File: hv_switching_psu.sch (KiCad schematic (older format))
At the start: 19 parts, among them P1 CONN_2, P2 CONN_2, P3 CONN_2, P4 CONN_1, SW1 SWITCH_INV, T1 IRF644PBF, U1 MAX1771

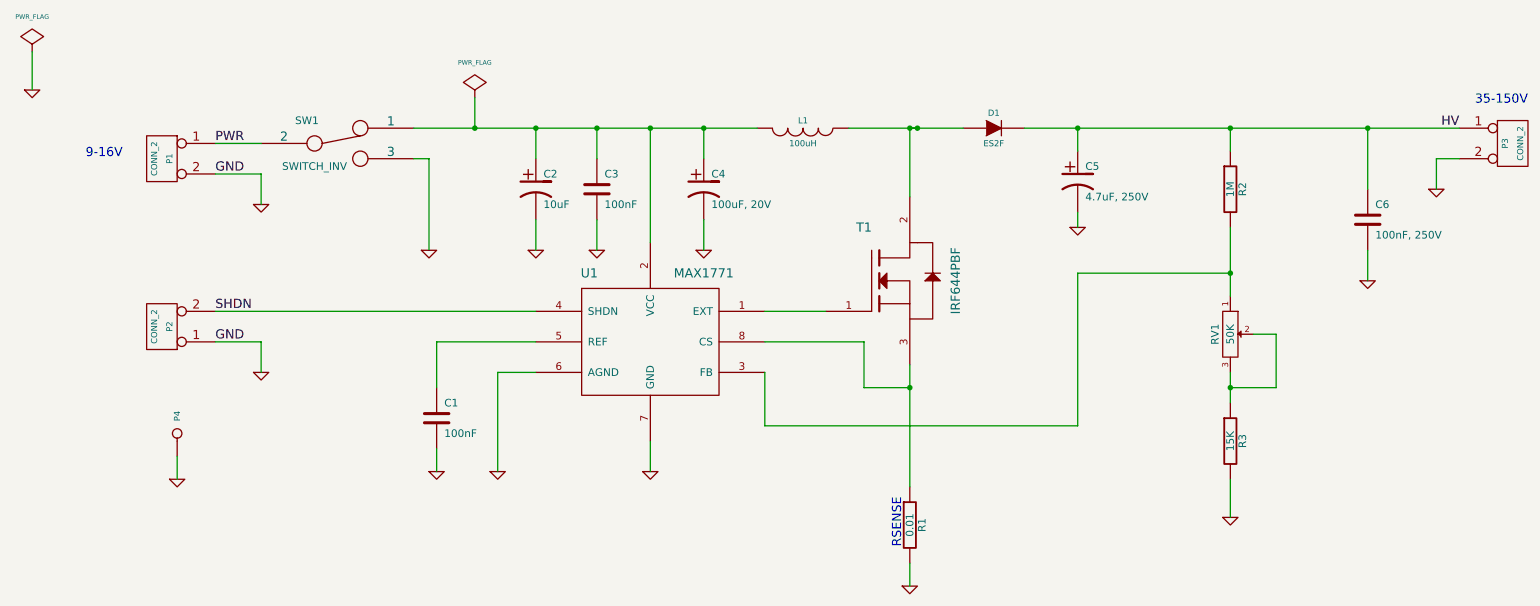
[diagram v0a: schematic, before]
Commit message: Modified annotations on schematic - changes input and output ranges.
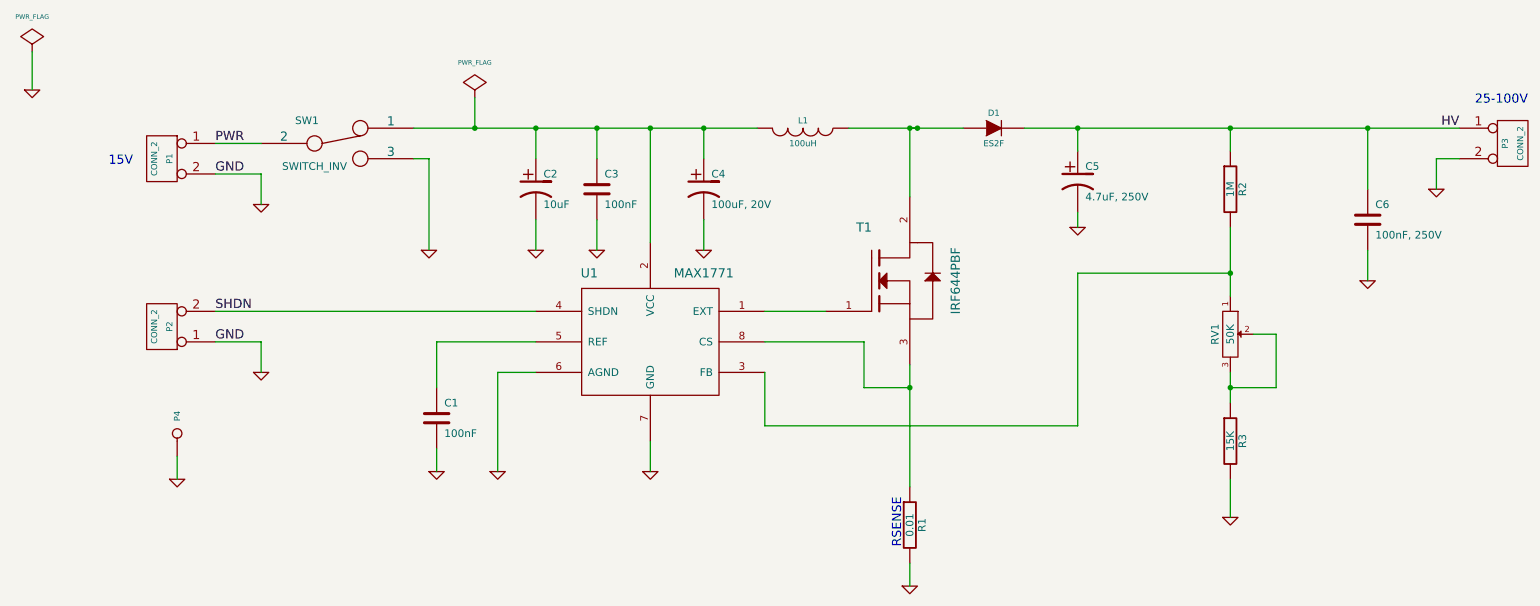
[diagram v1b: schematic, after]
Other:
- note added: "15V"
- note added: "25-100V"
- note removed: "35-150V"
- note removed: "9-16V"
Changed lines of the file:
@@
-EESchema Schematic File Version 2  date Fri 24 May 2013 06:33:11 PM PDT
+EESchema Schematic File Version 2  date Fri 24 May 2013 06:48:56 PM PDT
 LIBS:power
 LIBS:device
@@
 $EndComp
 Text Notes 10850 1450 2    60   ~ 0
-35-150V
+25-100V
 Text Label 10400 1600 2    60   ~ 0
 HV
@@
 	1    0    0    -1
 $EndComp
-Text Notes 1400 1800 0    60   ~ 0
-9-16V
+Text Notes 1550 1850 0    60   ~ 0
+15V
 Text Label 2250 1700 0    60   ~ 0
 PWR

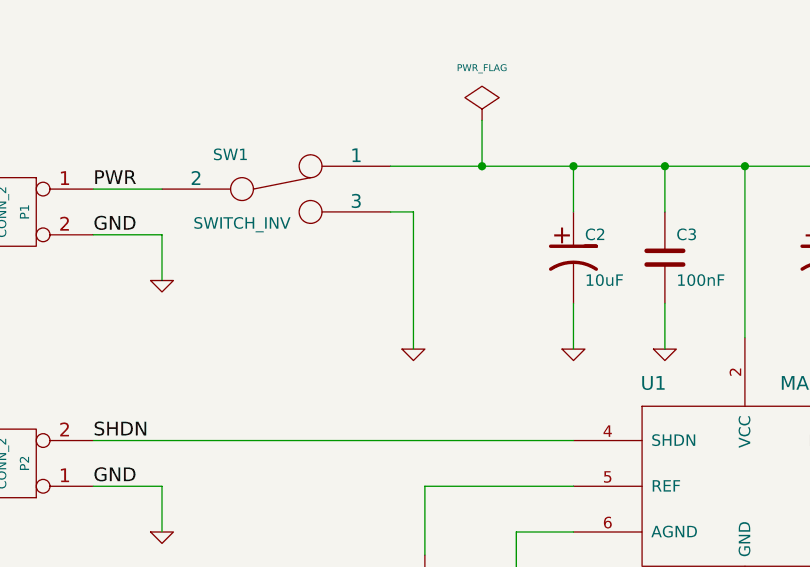
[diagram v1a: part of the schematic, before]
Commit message: Added version 1.4 of design - fixed issue with switch.
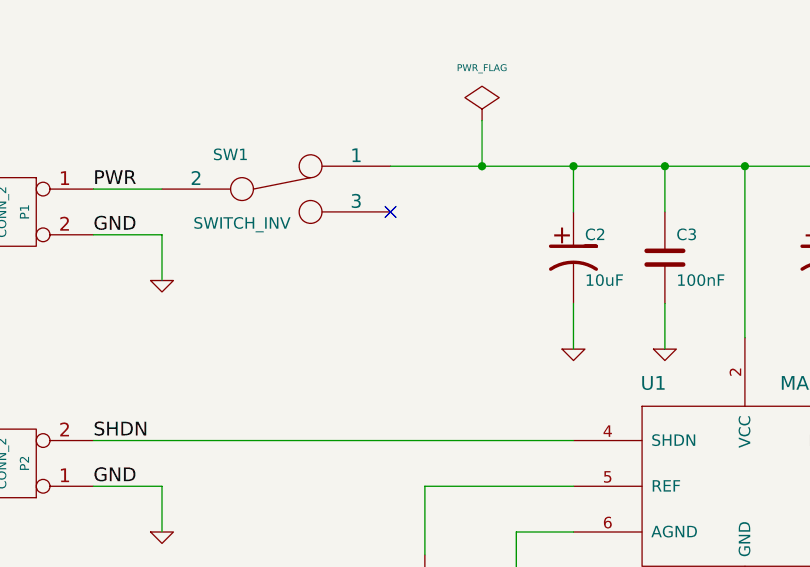
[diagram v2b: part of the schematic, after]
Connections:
- net GND: no longer SW1.3
- no-connect marks 0 -> 1
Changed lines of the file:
@@
-EESchema Schematic File Version 2  date Fri 24 May 2013 06:48:56 PM PDT
+EESchema Schematic File Version 2
 LIBS:power
 LIBS:device
@@
 Sheet 1 1
 Title ""
-Date "25 may 2013"
+Date "21 jan 2015"
 Rev ""
 Comp ""
@@
 Wire Wire Line
 	5450 2200 5450 2400
-Wire Wire Line
-	3650 2400 3650 1800
-Wire Wire Line
-	3650 1800 3550 1800
 Wire Wire Line
 	2250 1900 2550 1900
@@
 $EndComp
 $Comp
-L GND #PWR015
-U 1 1 50622416
-P 3650 2400
-F 0 "#PWR015" H 3650 2400 30  0001 C CNN
-F 1 "GND" H 3650 2330 30  0001 C CNN
-F 2 "" H 3650 2400 60  0001 C CNN
-F 3 "" H 3650 2400 60  0001 C CNN
-	1    3650 2400
-	1    0    0    -1
-$EndComp
-$Comp
 L SWITCH_INV SW1
 U 1 1 506223F0
@@
 	1    0    0    -1
 $EndComp
+NoConn ~ 3550 1800
 $EndSCHEMATC
